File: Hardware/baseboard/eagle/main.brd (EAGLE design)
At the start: 359.1 x 120.5 mm, 178 parts, among them J1 MICROUSB-FEM, X1 JST-4POS-2X4POS, X1.2 TACH/LAP, X2.1 MOTOR, X2.2 VRAILS+, X2.3 5V+SoC

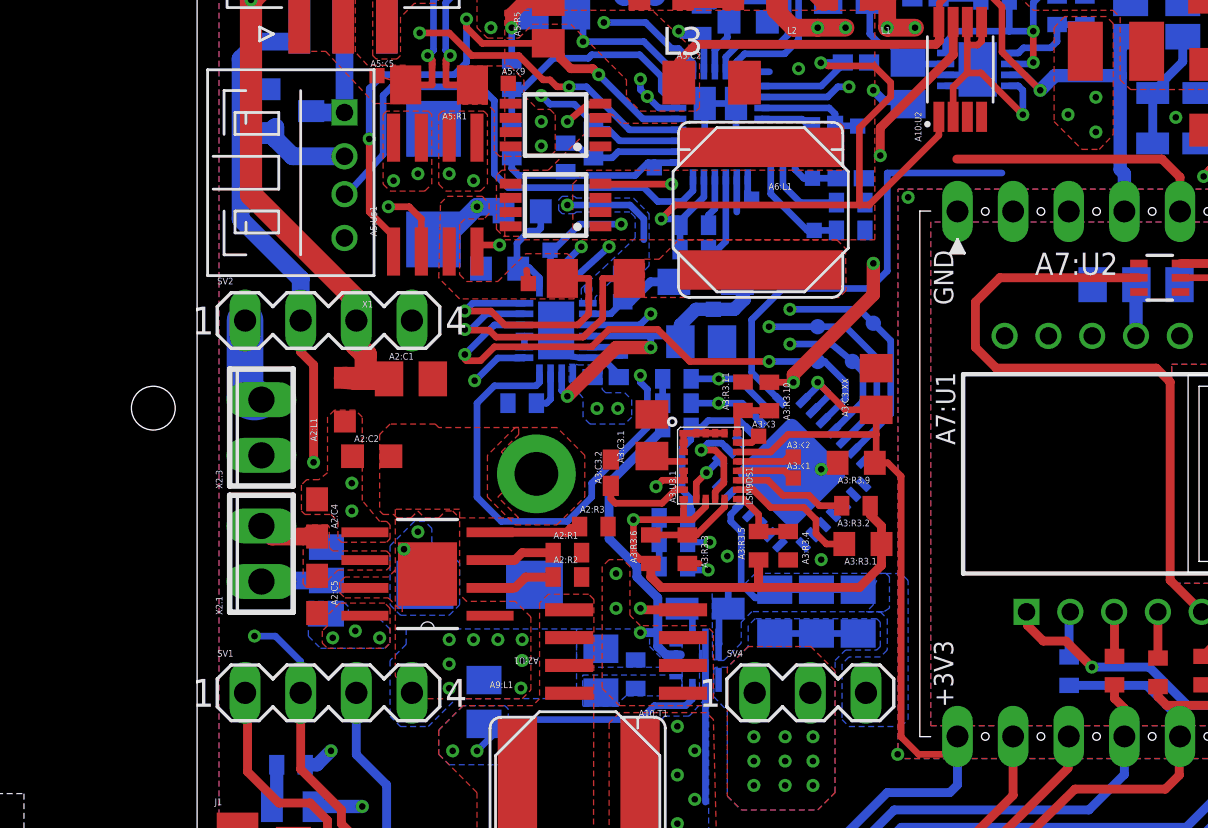
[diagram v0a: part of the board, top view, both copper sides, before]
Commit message: wip baseboard: 17 airwires, DRC checks out for most signals!
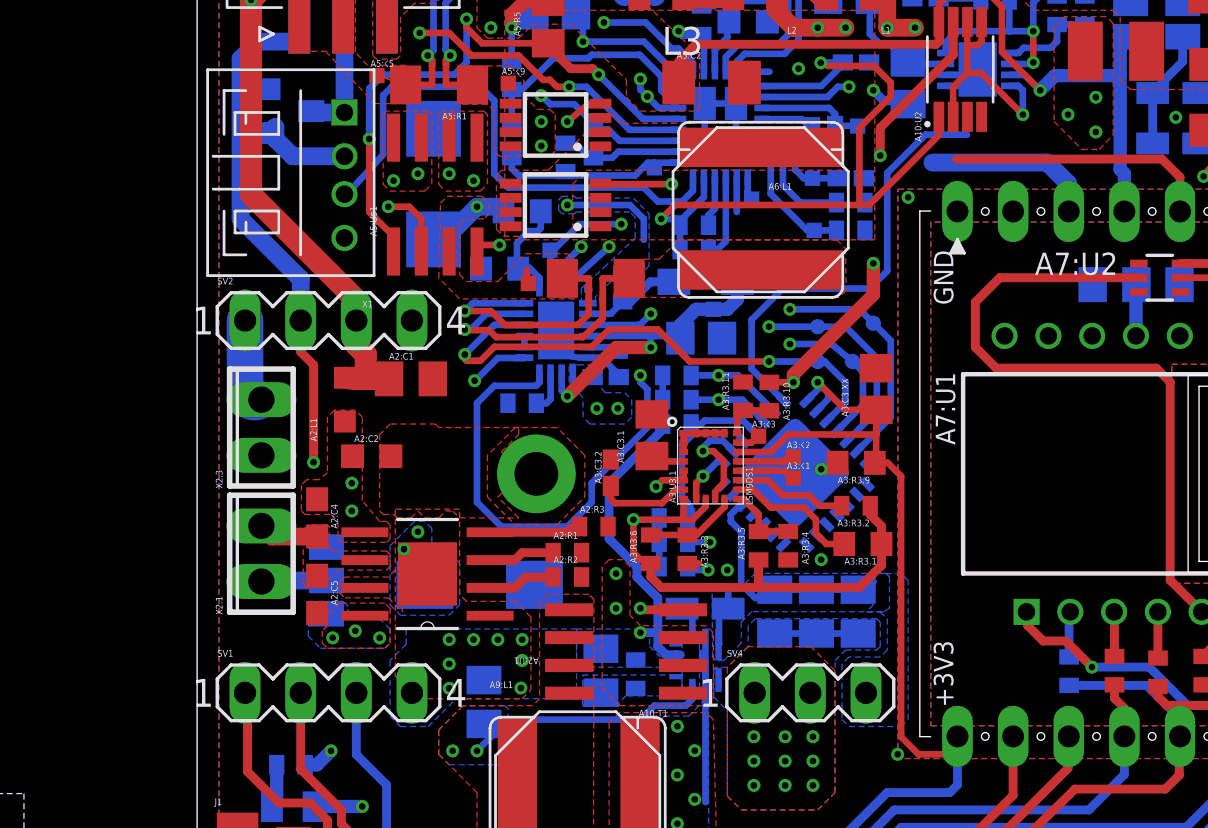
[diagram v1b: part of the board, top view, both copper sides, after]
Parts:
- moved A8:R3 0.16 mm to (26.9, 49.5)
- moved A6:C2 0.16 mm to (28.0, 51.2)
- moved A8:IC1 0.16 mm to (32.3, 45.1)
- moved A8:R1 0.16 mm to (26.9, 48.4)
- moved A8:R5 0.16 mm to (26.9, 47.3)
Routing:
- net SYSTWI.SDA: track 91.8 -> 116.4 mm, vias 2 -> 1
- net +5V: track 52.8 -> 61.0 mm
- net +3V3: track 92.3 -> 93.8 mm
- net A8:A1: track 12.7 -> 14.0 mm
- net SYSTWI.SCL: track 116.7 -> 117.9 mm
- net TOP.!RST: track 40.1 -> 39.3 mm
- net A6:↔ILIM: track 16.9 -> 16.1 mm
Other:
- board text removed: "->check out later"
- board text removed: "Unexpected Opportunity for built in high side shunt trace to measure power draw"
- board text removed: "[eq1]: V(in,max) = 30V"
- board text removed: "can't have a perfect design - will match length later using meander tool - maybe simulate if someone feels the need to"
- board text removed: "reduced by half :]"
- board text removed: "unimportant"

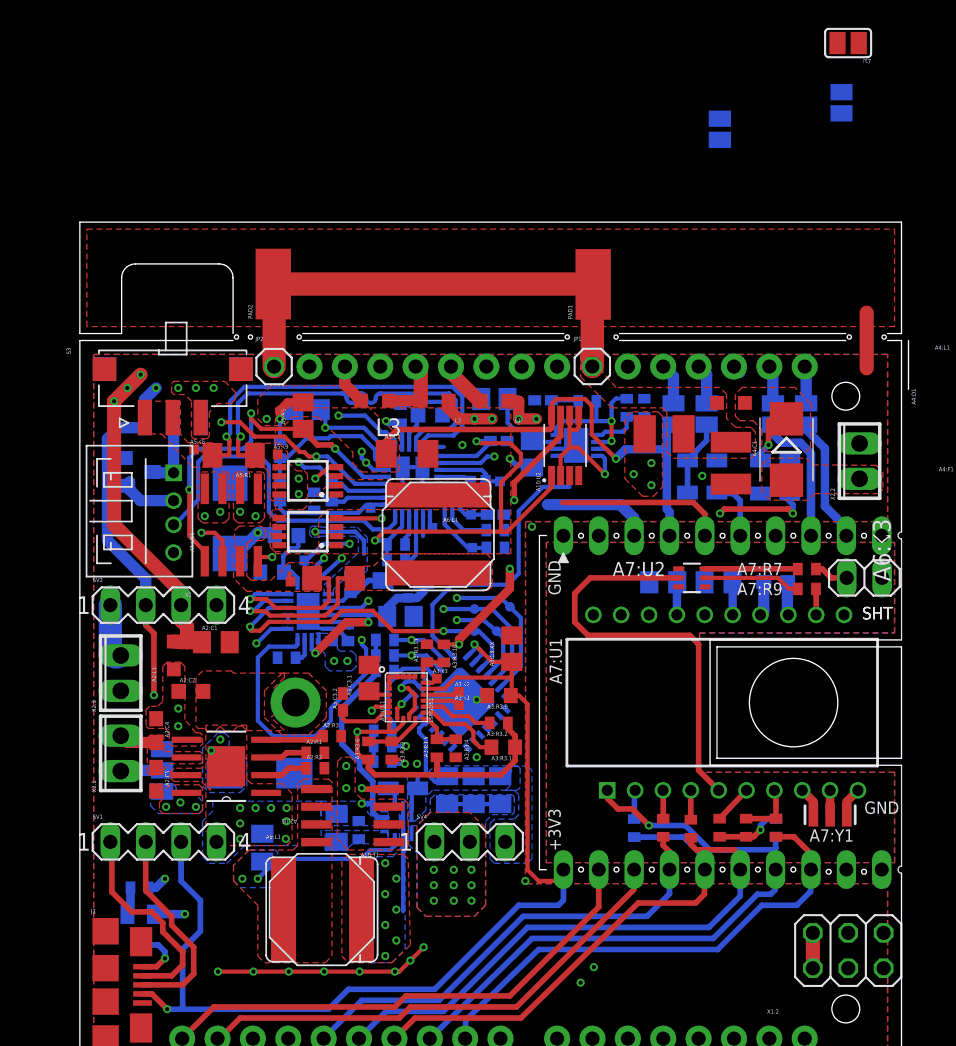
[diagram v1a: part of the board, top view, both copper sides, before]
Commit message: redid motor driver area
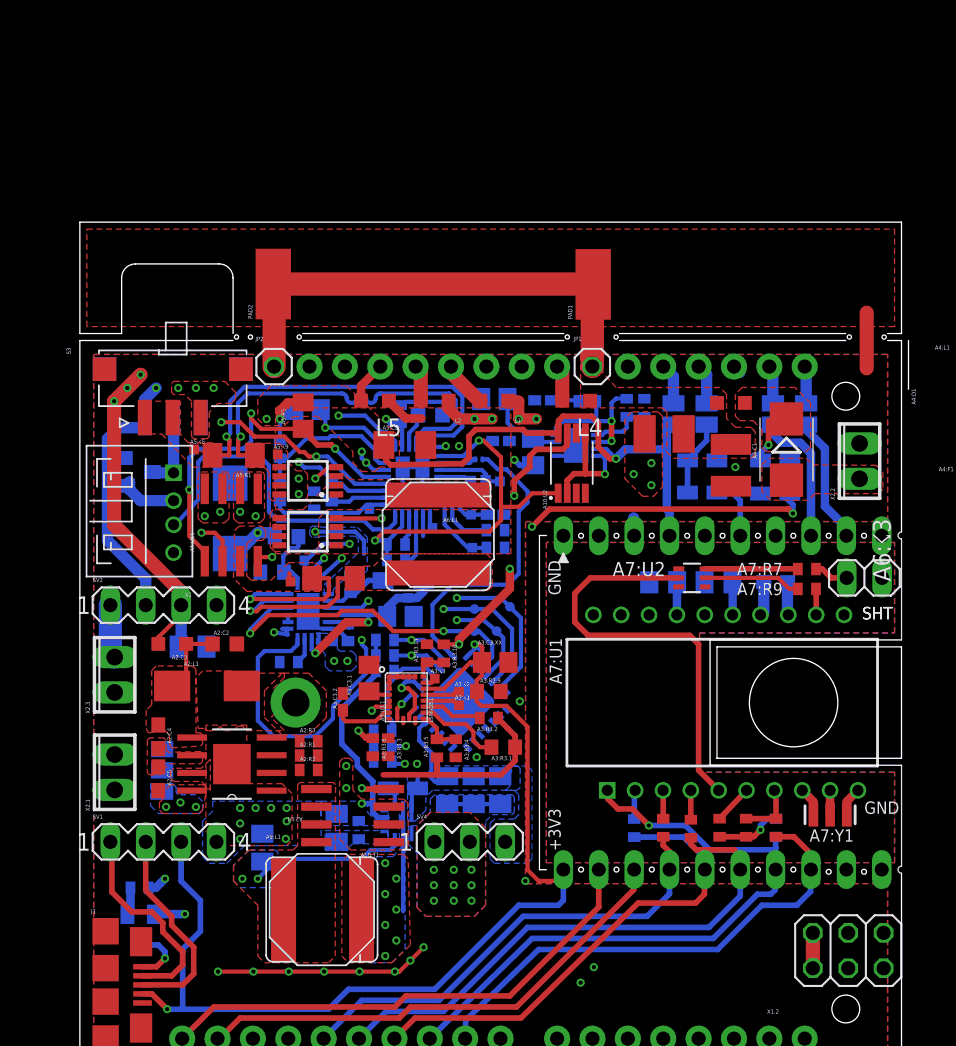
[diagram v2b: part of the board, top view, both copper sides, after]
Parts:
- removed ☈12, ☈7, ☈8: (no value), jumper:SJ
- added L4: BEAD/0R/⎵, rcl:L2012C
- added R2: (no value), rcl:R0201
- moved A2:C3 7.31 mm to (14.1, 46.2), flipped to the top, turned to 0 degrees
- moved A2:C2 4.18 mm to (15.4, 49.2)
- moved A2:R3 1.72 mm to (21.4, 42.2)
- moved A2:C1 1.70 mm to (13.1, 49.0), flipped to the bottom, turned to 180 degrees
- moved A3:C3.XX 1.54 mm to (34.8, 47.9), turned to 0 degrees
- moved X2.1 1.42 mm to (7.50, 40.0)
- moved A10:U2 1.36 mm to (40.3, 62.2)
- moved A2:L1 0.84 mm to (11.6, 49.2), turned to 180 degrees
- moved A3:R3.2 0.80 mm to (34.4, 43.9)
- moved A3:R3.9 0.78 mm to (34.4, 45.8), turned to 0 degrees
- moved A5:C2 0.65 mm to (28.3, 63.5)
- moved A2:R1 0.52 mm to (21.4, 41.2)
- moved A2:R2 0.49 mm to (21.4, 40.2)
- moved A2:C4 0.47 mm to (10.6, 42.5)
- moved X2.3 0.45 mm to (7.50, 47.0)
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- renumbered L3 to L5
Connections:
- removed net +9V: ☈7.1
- removed net UNO.IOREF: L5.2, XA1.I/OREF
- net !RST: now also R2.2; no longer ☈12.1
- net +18V: now also L4.1
- net TOP.!RST: now also L5.1, R2.1; no longer ☈12.2, ☈8.1
- net UNO.3V3: no longer L5.1
- net UNO.RESET: now also L5.2; no longer ☈8.2
- net UNO.VIN: now also L4.2; no longer ☈7.2
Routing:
- net TOP.RRX: track 35.5 -> 61.7 mm, vias 4 -> 3
- net TOP.!RST: track 39.3 -> 31.7 mm
- net +3V3: track 93.8 -> 87.1 mm
- net +5V: track 61.0 -> 54.4 mm
- net A2:VM: track 0.00 -> 5.32 mm, vias 4 -> 0
- net TOP.PWRON: track 34.7 -> 29.7 mm
- net A3:SDO_AG: track 4.55 -> 0.35 mm
- net A2:ILIM: track 4.20 -> 0.00 mm
- net PWR.MOTB: track 3.09 -> 0.00 mm
- net ✳TOP.MOT-: track 3.08 -> 0.00 mm
- net PWR.MOTA: track 3.02 -> 0.00 mm
- net UNO.IOREF: track 2.94 -> 0.00 mm
- net ✳TOP.MOT+: track 2.74 -> 0.00 mm
- net UNO.VIN: track 0.00 -> 2.61 mm
- net UNO.3V3: track 5.18 -> 2.90 mm
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- removed copper zone on layer 15, net A2:VM
- removed copper zone on layer 16, net A2:VM

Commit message: commit message
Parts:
- removed SJ1: (no value), jumper:SJ_2
- removed X2.1: MOTOR, con-phoenix-254:2POL254
- added X2: (no value), con-phoenix-254:3POL254
- A8:R2, A8:R4, A8:R6: device rcl:R0402 -> rcl:R0201
- moved A8:R4 9.14 mm to (27.8, 49.8), flipped to the top, turned to 180 degrees
- moved A8:R2 6.94 mm to (27.8, 48.7), flipped to the top, turned to 180 degrees
- moved A8:R6 4.91 mm to (27.8, 47.8), flipped to the top, turned to 180 degrees
- moved A2:R3 4.63 mm to (17.1, 44.0), turned to 180 degrees
- moved R2 4.10 mm to (33.0, 66.5)
- moved A5:R9 3.42 mm to (31.4, 55.9), turned to 90 degrees
- moved A5:☇6 2.88 mm to (30.3, 56.5)
- moved A5:R10 2.75 mm to (32.5, 55.9), turned to 90 degrees
- moved A3:R3.6 2.70 mm to (28.6, 42.7), turned to 0 degrees
- moved A3:C3.2 2.25 mm to (25.6, 43.6), turned to 180 degrees
- moved A6:C2 2.01 mm to (28.7, 53.1), turned to 90 degrees
- moved A6:D1 1.86 mm to (26.8, 52.6), turned to 270 degrees
- moved A6:☇5 1.59 mm to (28.6, 50.9)
- moved A6:☇7 1.50 mm to (34.6, 52.7)
- moved A3:R3.3 1.44 mm to (28.6, 41.6), turned to 180 degrees
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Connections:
- removed net ✳TOP.MOT-: SJ1.2, X2.1.1
- net GND: now also J1.M1, J1.M2, J1.S1, J1.S2, J1.S3, J1.S4, X2.2; no longer SJ1.1
- net TOP.MOT-: now also X2.1; no longer SJ1.3
- net ✳TOP.MOT+: now also X2.3; no longer X2.1.2
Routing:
- net UNO.RESET: track 27.0 -> 3.03 mm
- net TOP.RRX: track 61.7 -> 38.7 mm
- net +4.1V: track 84.3 -> 61.6 mm
- net A8:A2: track 17.4 -> 5.10 mm, vias 2 -> 1
- net +5V: track 54.4 -> 66.5 mm
- net !RST: track 2.75 -> 14.1 mm
- net A8:A1: track 14.0 -> 4.37 mm, vias 2 -> 1
- net A10.!ACT: track 40.0 -> 31.9 mm
- net TOP.!RST: track 31.7 -> 38.8 mm, vias 0 -> 1
- net +3V3: track 87.1 -> 80.0 mm
- net A8:A0: track 8.72 -> 3.70 mm, vias 0 -> 1
- net GND: track 48.2 -> 44.9 mm
- net TOP.MODE: track 27.2 -> 24.2 mm
- net A3:↔C1: track 4.25 -> 1.31 mm
- net PWR.MOTA: track 0.00 -> 2.67 mm
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- removed copper zone on layer 15, net TOP.MOT-
- removed copper zone on layer 16, net TOP.MOT-
- removed copper zone on layer 2, net TOP.MOT-

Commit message: commmit message
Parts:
- moved R2 4.36 mm to (32.2, 62.2)
- moved A5:R2 0.93 mm to (27.1, 65.9), turned to 0 degrees
- moved A10:U2 0.51 mm to (39.8, 62.2), turned to 0 degrees
- moved A5:C2 0.50 mm to (28.0, 63.3)
- moved A10:R2 0.16 mm to (44.4, 66.2)
- moved A10:R7 0.16 mm to (45.7, 66.2)
- moved A10:U1 0.16 mm to (40.8, 63.5)
- moved A5:R3 0.16 mm to (21.5, 66.0)
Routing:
- net TOP.RRX: track 38.7 -> 61.9 mm, vias 3 -> 2
- net SYSTWI.!INT: track 79.5 -> 62.7 mm
- net +5V: track 66.5 -> 53.0 mm
- net !RST: track 14.1 -> 1.19 mm
- net A10.!ACT: track 31.9 -> 25.7 mm, vias 2 -> 1
- net TOP.!RST: track 38.8 -> 35.1 mm
- net +4.1V: track 61.6 -> 64.1 mm
- net +3V3: track 80.0 -> 82.3 mm
- net TOP.PWRON: track 29.6 -> 27.6 mm
- net ITH: track 19.0 -> 20.6 mm
- net VDD: track 48.5 -> 46.9 mm
- net +18V: track 96.9 -> 95.8 mm
- net GND: vias 33 -> 31

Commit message: -
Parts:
- moved A7:R4 1.93 mm to (50.8, 36.3)
- moved A7:R5 1.31 mm to (52.2, 36.3)
- moved A3:C3.XX 1.00 mm to (33.9, 47.6)
- moved A7:R3 1.00 mm to (47.8, 36.3)
- moved A5:C6 0.99 mm to (33.6, 58.6), turned to 180 degrees
- moved A5:☇7 0.97 mm to (32.9, 57.5)
- moved A6:☇7 0.95 mm to (33.7, 52.7)
- moved A7:U2 0.95 mm to (49.9, 54.0)
- moved A6:☇9 0.93 mm to (33.8, 50.9)
- moved A7:R8 0.71 mm to (55.6, 36.3)
- moved A7:R6 0.71 mm to (53.5, 36.3)
- moved A10:U2 0.50 mm to (39.7, 62.7)
- moved A6:☇6 0.48 mm to (32.9, 51.7)
- moved A6:☇8 0.48 mm to (32.9, 50.1)
- moved A3:R3.9 0.32 mm to (34.4, 45.5)
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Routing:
- net +5V: track 53.0 -> 88.6 mm, vias 4 -> 7
- net TOP.!RST: track 35.1 -> 66.6 mm
- net SYSTWI.!INT: track 62.7 -> 90.0 mm
- net A10.!ACT: track 25.7 -> 45.1 mm, vias 1 -> 2
- net +4.1V: track 64.1 -> 81.8 mm
- net TOP.RRX: track 61.9 -> 66.7 mm
- net MOSI: track 38.9 -> 37.2 mm
- net TOP.PGOOD: track 26.3 -> 24.8 mm
- net +3V3: track 82.3 -> 83.7 mm
- net A10:REF: track 11.4 -> 10.1 mm
- net A7:U1.MOSI: track 2.11 -> 3.36 mm
- net A7:N$1: track 6.69 -> 5.73 mm
- net A7:LEDCTRL: track 30.6 -> 31.6 mm
- net A7:RST: track 2.81 -> 1.99 mm
- net A10:BATOK: track 9.50 -> 8.72 mm
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
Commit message: -
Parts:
- removed SV4: (no value), con-lstb:MA03-1
- moved X1.2 0.75 mm to (60.0, 27.9)
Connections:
- removed net !INT: XA1.IO.8
- new net N$5: XA1.IO.4
- new net N$8: XA1.IO.1
- net +5V: no longer SV4.3
- net GND: no longer SV4.1, SV4.2
- net LAP: now also XA1.IO.2
- net PWR.MOTA: now also XA1.IO.5
- net PWR.MOTB: now also XA1.IO.6
- net SYSTWI.!INT: now also XA1.IO.8
- net TACH: now also XA1.IO.3
- net TOP.RRX: now also XA1.IO.0; no longer XA1.IO.7
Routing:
- net PWR.MOTB: track 2.64 -> 44.0 mm, vias 0 -> 1
- net PWR.MOTA: track 2.67 -> 40.4 mm, vias 0 -> 1
- net +5V: track 88.6 -> 53.4 mm, vias 7 -> 5
- net TACH: track 0.00 -> 17.8 mm
- net GND: track 44.9 -> 31.9 mm, vias 31 -> 29
- net TOP.RRX: track 66.7 -> 54.5 mm
- net LAP: track 0.00 -> 10.8 mm
- net SYSTWI.!INT: track 90.0 -> 100.5 mm, vias 2 -> 3
- net SYSTWI.SCL: track 117.9 -> 120.0 mm
- net SYSTWI.SDA: track 116.4 -> 118.1 mm
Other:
- outline, holes or cut-outs redrawn
- board text removed: "TODO"

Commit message: …
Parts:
- added A9:R3: 100kR/⎵, resistor:R0402
- moved A2:R2 1.85 mm to (23.0, 42.1), turned to 45 degrees
- moved A5:☇4 1.27 mm to (24.5, 58.9)
- moved A2:R1 1.12 mm to (22.2, 42.9), turned to 45 degrees
- moved R1 0.88 mm to (8.45, 32.0), turned to 270 degrees
- moved A3:C3.2 0.22 mm to (25.4, 43.7)
- moved A2:C3 0.16 mm to (14.1, 46.4)
- moved A2:C2 0.16 mm to (15.4, 49.4)
- moved A2:L1 0.16 mm to (11.6, 49.4)
- moved A3:R3.3 0.16 mm to (28.6, 41.8)
- moved A3:R3.6 0.16 mm to (28.6, 42.9)
- moved A9:R1 0.16 mm to (28.2, 39.0)
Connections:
- removed net A7:MRXS: A7:⌁11.P$1
- removed net A7:MTXS: A7:⌁12.P$1
- removed net N$8: XA1.IO.1
- removed net TOP.EN: A9:U1.7
- new net TOP.MTXS: A7:⌁12.P$1, XA1.IO.1
- net GND: now also A9:R3.1
- net PWR.MOTA: now also A2:R2.1, A2:U1.2; no longer A2:R1.1, A2:U1.3
- net PWR.MOTB: now also A2:R1.1, A2:U1.3; no longer A2:R2.1, A2:U1.2
- net TOP.RRX: now also A7:⌁11.P$1
- net TOP.VSYS/GUARD: now also A9:R3.2, A9:U1.7
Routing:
- net TOP.RRX: track 54.5 -> 97.9 mm
- net +5V: track 53.4 -> 83.9 mm
- net PWR.MOTA: track 40.4 -> 60.4 mm, vias 1 -> 3
- net PWR.MOTB: track 44.0 -> 61.4 mm, vias 1 -> 3
- net TOP.MTXS: track 0.00 -> 14.8 mm
- net +3V3: track 83.7 -> 72.5 mm, vias 7 -> 9
- net TOP.VSYS/GUARD: track 11.5 -> 21.3 mm, vias 2 -> 3
- net +4.1V: track 81.8 -> 85.9 mm, vias 6 -> 5
- net A10:REF: track 10.1 -> 11.8 mm
- net A6:BG: track 13.4 -> 12.2 mm
- net SYSTWI.SDA: track 118.1 -> 119.2 mm
- net SYSTWI.SCL: track 120.0 -> 121.1 mm
- net MISO: track 34.0 -> 34.8 mm
- net TOP.RUN: track 24.9 -> 24.2 mm
- net GND: vias 29 -> 28
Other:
- board size 359.1 x 120.5 mm -> 108.5 x 120.5 mm
- board text removed: "200mm grid shift ripping up gets old pretty quickly"
- board text removed: ">to sysctrl<"
- board text removed: "AREA 1 REAL ESTATE"
- board text removed: "AREA 4-B: LOGIC/Control"
- board text removed: "FIND ALTPART"
- board text removed: "Important design note: Power components must be on top layer: -> airflow and passive cooling"
- board text removed: "MAX"
- board text removed: "MAXIMIZE"
- board text removed: "RATING!"
- board text removed: "ROOM"
- board text removed: "SoC"
- board text removed: "maximize/poly"
- board text removed: "move bridges/beads (to bottom?)"
- board text removed: "vrails"
